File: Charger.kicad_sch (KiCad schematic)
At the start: 61 parts, among them Q6 BSC0702LS, Q7 BSC0702LS, Q8 BSC0702LS, Q9 BSC0702LS, U27 BQ25756RRVR

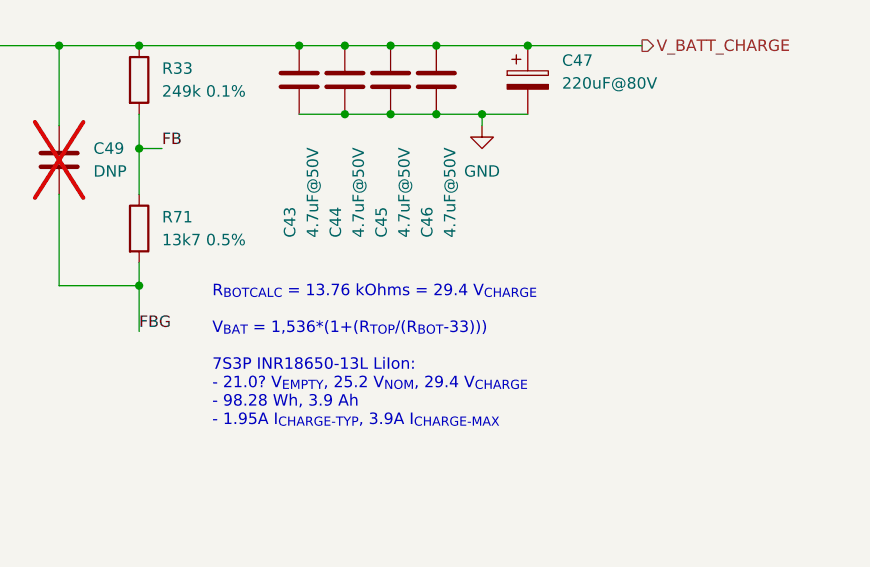
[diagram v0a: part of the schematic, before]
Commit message: Change Vbat target to 28.28V
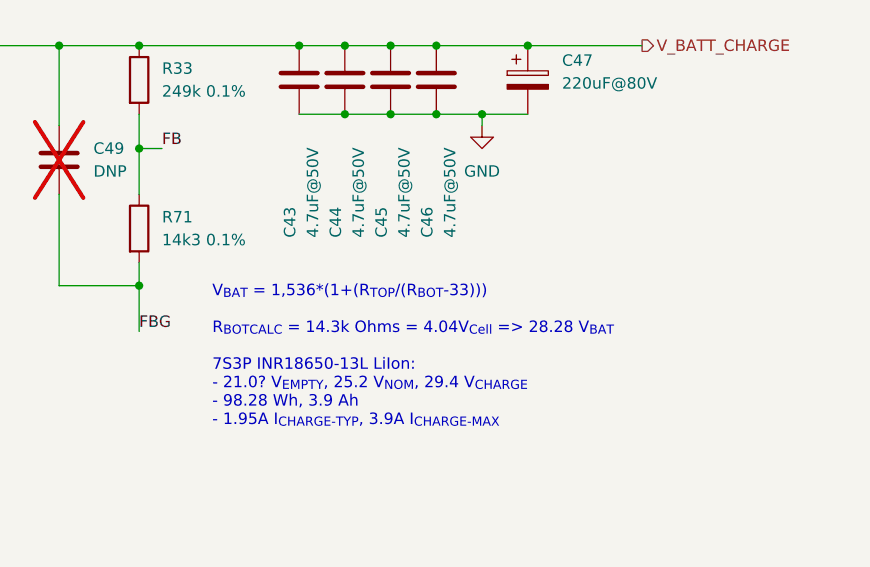
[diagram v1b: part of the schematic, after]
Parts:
- R71: value 13k7 0.5% -> 14k3 0.1%; LCSC Part # C407628 -> C861131; PN 0603WAD1372T5E -> RT0603BRD0714K3L
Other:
- note added: "V_{BAT} = 1,536*(1+(R_{TOP}/(R_{BOT}-33))) R_{BOTCALC} = 14.3k Ohms = 4.04V_{Cell} => 28.28 V_{BAT} 7S3P INR18650-13L LiIon: - 21.0? V_{EMPTY}, 25.2 V_{NOM}, 29.4 V_{CHARGE} - 98.28 Wh, 3.9 Ah - 1.95A I_{CHARGE-TYP}, 3.9A I_{CHARGE-MAX}"
- note removed: "R_{BOTCALC} = 13.76 kOhms = 29.4 V_{CHARGE} V_{BAT} = 1,536*(1+(R_{TOP}/(R_{BOT}-33))) 7S3P INR18650-13L LiIon: - 21.0? V_{EMPTY}, 25.2 V_{NOM}, 29.4 V_{CHARGE} - 98.28 Wh, 3.9 Ah - 1.95A I_{CHARGE-TYP}, 3.9A I_{CHARGE-MAX}"
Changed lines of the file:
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@@
 		)
 	)
-	(text "R_{BOTCALC} = 13.76 kOhms = 29.4 V_{CHARGE}\n\nV_{BAT} = 1,536*(1+(R_{TOP}/(R_{BOT}-33)))\n\n7S3P INR18650-13L LiIon:\n- 21.0? V_{EMPTY}, 25.2 V_{NOM}, 29.4 V_{CHARGE}\n- 98.28 Wh, 3.9 Ah\n- 1.95A I_{CHARGE-TYP}, 3.9A I_{CHARGE-MAX}"
+	(text "V_{BAT} = 1,536*(1+(R_{TOP}/(R_{BOT}-33)))\n\nR_{BOTCALC} = 14.3k Ohms = 4.04V_{Cell} => 28.28 V_{BAT}\n\n7S3P INR18650-13L LiIon:\n- 21.0? V_{EMPTY}, 25.2 V_{NOM}, 29.4 V_{CHARGE}\n- 98.28 Wh, 3.9 Ah\n- 1.95A I_{CHARGE-TYP}, 3.9A I_{CHARGE-MAX}"
 		(exclude_from_sim no)
 		(at 342.138 166.624 0)
@@
 			)
 		)
-		(property "Value" "13k7 0.5%"
+		(property "Value" "14k3 0.1%"
 			(at 336.55 153.6699 0)
 			(show_name no)
@@
 			)
 		)
-		(property "Description" "100mW Thick Film Resistors 75V ±100ppm/℃ ±0.5% 13.7kΩ 0603 Chip Resistor"
+		(property "Description" "-55℃~+155℃ 100mW 14.3kΩ 75V Thin Film Resistor ±0.1% ±25ppm/℃ 0603 Chip Resistor - Surface Mount ROHS"
 			(at 334.01 152.4 0)
 			(hide yes)
@@
 			)
 		)
-		(property "PN" "0603WAD1372T5E"
+		(property "PN" "RT0603BRD0714K3L"
 			(at 334.01 152.4 0)
 			(hide yes)
@@
 			)
 		)
-		(property "LCSC Part #" "C407628"
+		(property "LCSC Part #" "C861131"
 			(at 334.01 152.4 0)
 			(hide yes)

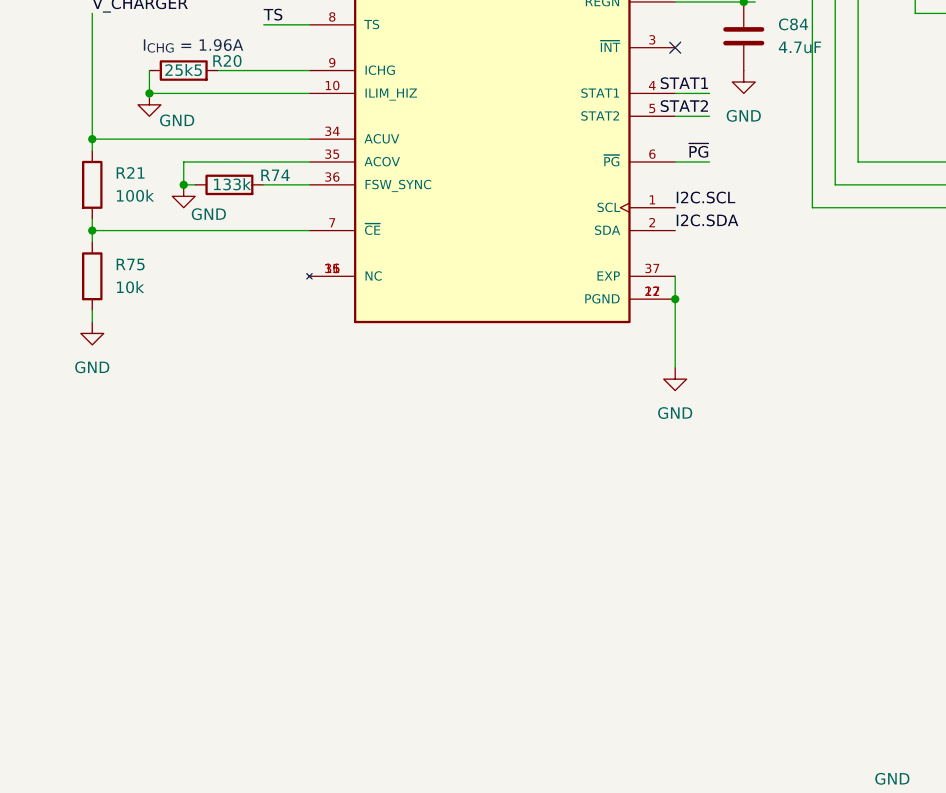
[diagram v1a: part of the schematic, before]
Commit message: Optional 6-9A charge current via Fsw 200kHz solder jumper
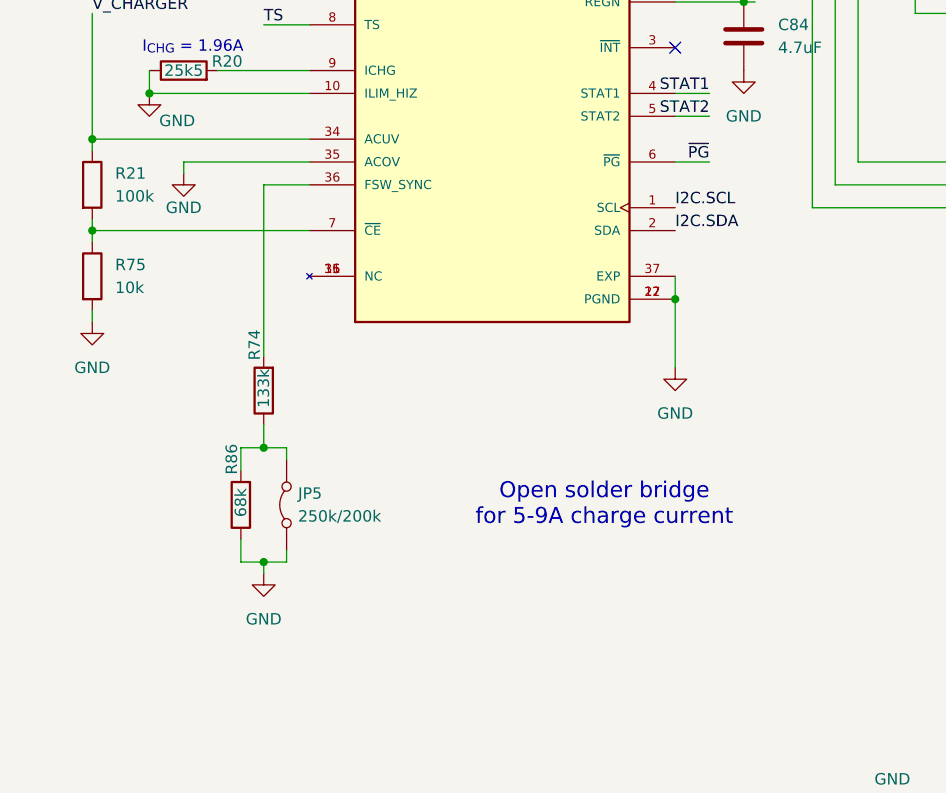
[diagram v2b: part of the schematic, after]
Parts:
- added JP5: 250k/200k, Jumper:SolderJumper-2_P1.3mm_Bridged_RoundedPad1.0x1.5mm, symbol Jumper:Jumper_2_Bridged
- added R86: 68k, Resistor_SMD:R_0603_1608Metric, symbol Device:R
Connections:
- net GND: now also JP5.1 (A), R86.1; no longer R74.1
- new net: JP5.2 (B), R74.1, R86.2
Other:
- note added: "Open solder bridge for 5-9A charge current"
- moved on the sheet: R74
